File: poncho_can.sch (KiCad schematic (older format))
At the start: 15 parts

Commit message: Agrego la proteccion en el esquematico
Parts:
- removed J? (x4): GS2, Connectors:GS2, symbol GS2
- removed J? (x2): DB9_Female, symbol DB9_Female
- removed R? (x2): R, symbol R
- removed U? (x2): TJA1051T, Housings_SOIC:SOIC-8_3.9x4.9mm_Pitch1.27mm, symbol TJA1051T
- added C? (x2): 47n, symbol C
- added C?: 100n, symbol C
- added D?: A00094, symbol A00094
- added J? (x2): GS2, Connectors:GS2, symbol GS2
- added J?: DB9_Male_MountingHoles, symbol DB9_Male_MountingHoles
- added R? (x4): 60, symbol R
- added U?: TJA1051T, Housings_SOIC:SOIC-8_3.9x4.9mm_Pitch1.27mm, symbol TJA1051T
- gave numbers to parts that had none: 4
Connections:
- wire segments 88 -> 89
- no-connect marks 46 -> 45
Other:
- moved on the sheet: J10, J7, J8, J9, XA101B

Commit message: Improved PCB
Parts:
- added C103, C104: 47n, Capacitors_SMD:C_0805_HandSoldering, symbol C
- added C106: 100n, Capacitors_SMD:C_0805_HandSoldering, symbol C
- added D102: RSB27C2, TO_SOT_Packages_SMD:SOT-23W_Handsoldering, symbol A00094
- added J102: DB9_Male_MountingHoles, Connect:DB9MC, symbol DB9_Male_MountingHoles
- added J105, J106: GS2, Connect:GS2, symbol GS2
- added R103, R104, R107, R108: 60, Resistors_SMD:R_0805_HandSoldering, symbol R
- added U102: TJA1051T, Housings_SOIC:SOIC-8_3.9x4.9mm_Pitch1.27mm, symbol TJA1051T
- C101, C102, C105: renamed from C?; footprint (none) -> Capacitors_SMD:C_0805_HandSoldering
- D101: renamed from D?; value A00094 -> RSB27C2; footprint (none) -> TO_SOT_Packages_SMD:SOT-23; ManufacturerPN D5V0L2B3W-7 -> (none); Reverse Working Voltage 5V -> (none); eAPN A00094 -> (none)
- J10, J7, J8, J9: footprint Connectors:GS2 -> Connect:GS2
- J101: renamed from J?; footprint (none) -> Connect:DB9MC
- J103, J104: renamed from J?; footprint Connectors:GS2 -> Connect:GS2
- R101, R102, R105, R106: renamed from R?; footprint (none) -> Resistors_SMD:R_0805_HandSoldering
- gave numbers to parts that had none: 1
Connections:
- net +5V: now also C106.1, U102.3 (VCC)
- net GND: now also C103.1, C104.2, C106.2, D102.3 (common), J102.3, U102.2 (GND)
- net at J8.2 (G2): now also U102.4 (RXD)
- net at J7.2 (G2): now also U102.1 (TXD)
- new net: D102.2 (A2), J102.2, R103.2, R104.2, U102.6 (CANL)
- new net: D102.1 (A1), J102.7, J105.1 (G1), J106.1 (G1), U102.7 (CANH)
- new net: J106.2 (G2), R108.1
- new net: J105.2 (G2), R107.1
- new net: C103.2, R103.1, R107.2
- new net: C104.1, R104.1, R108.2
- no-connect marks 45 -> 46

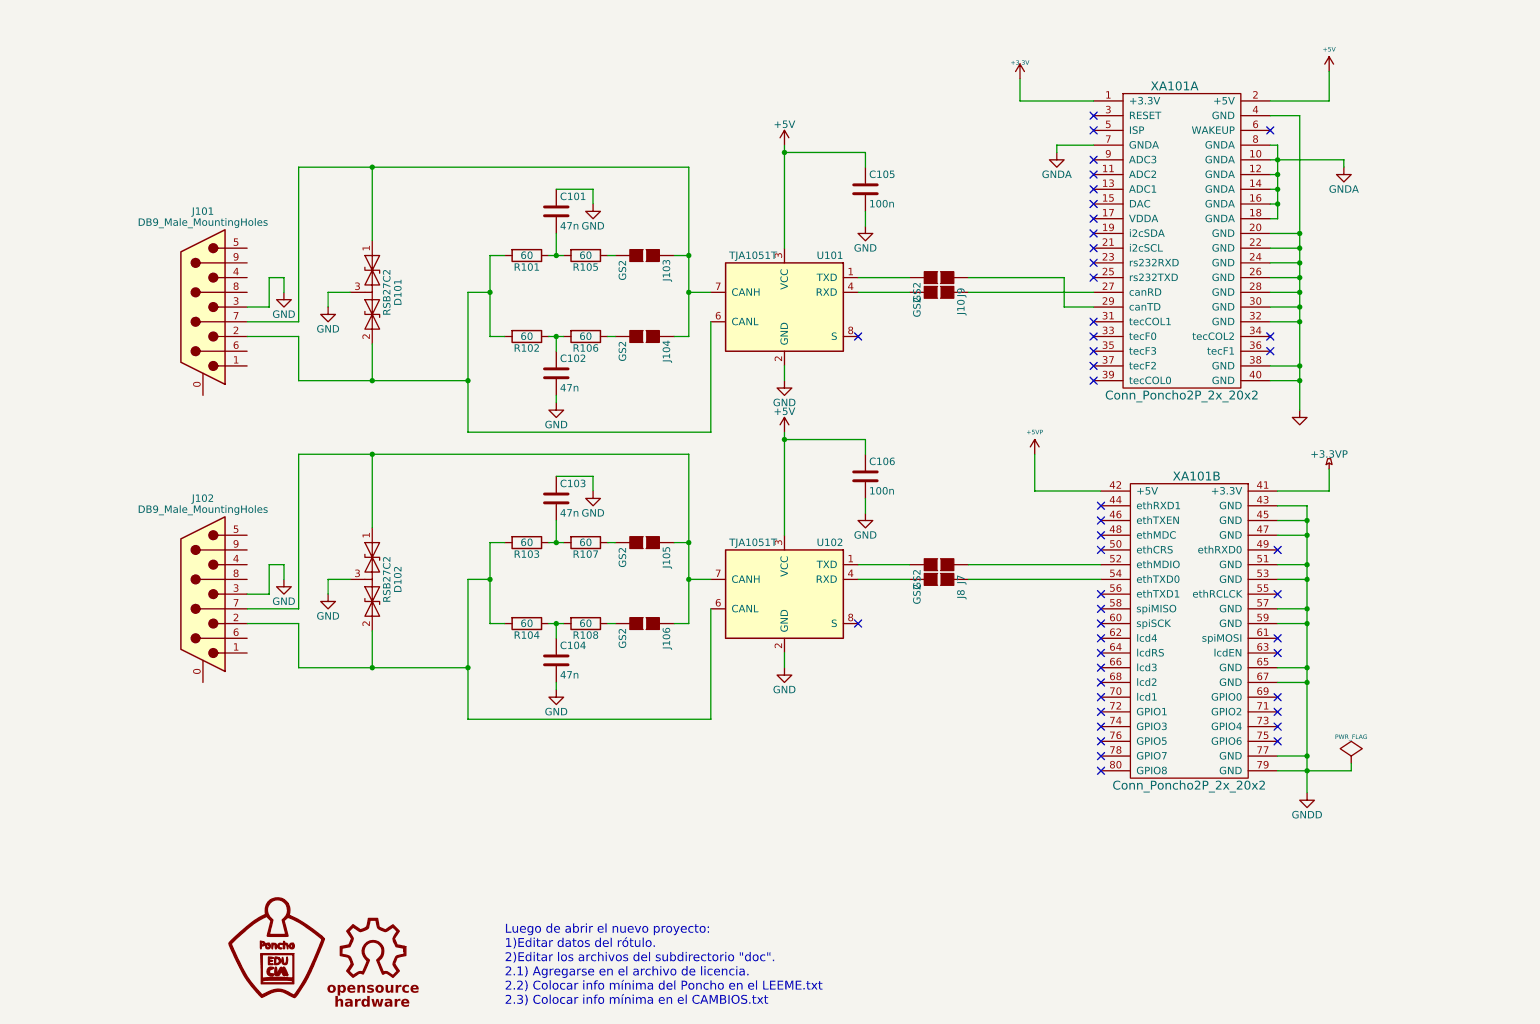
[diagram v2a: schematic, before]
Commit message: Cambio los jumpers de lugar en el esquematico y agrego leds en RX y TX
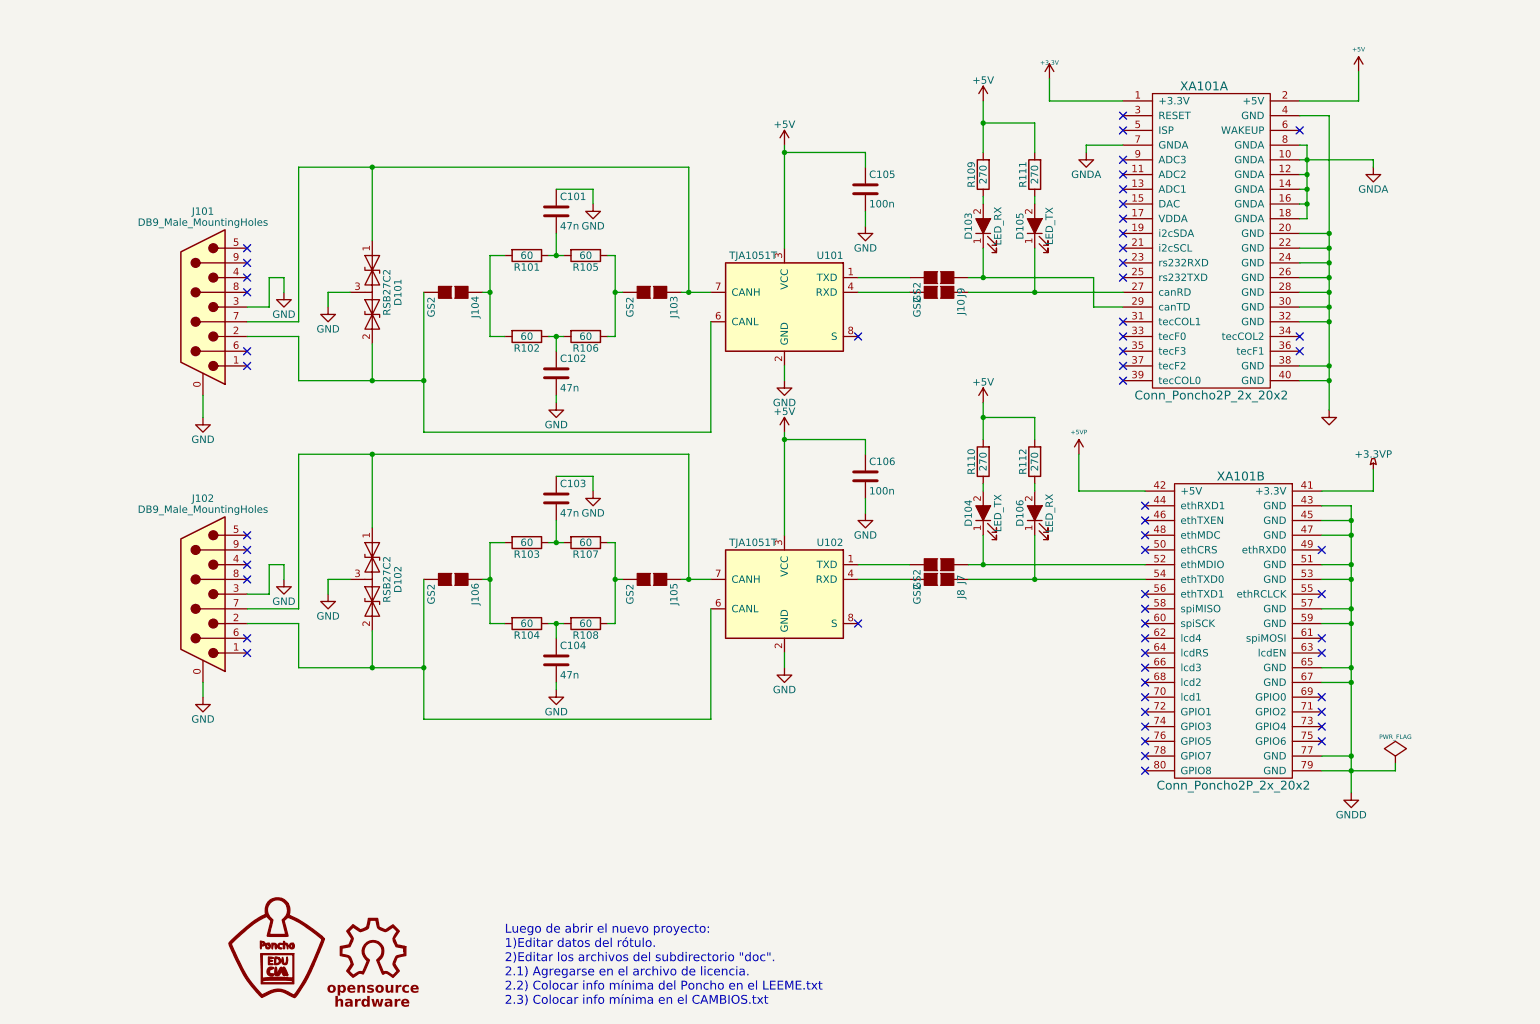
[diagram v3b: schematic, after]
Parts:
- added D103, D106: LED_RX, LEDs:LED_0805_HandSoldering, symbol LED_ALT
- added D104, D105: LED_TX, LEDs:LED_0805_HandSoldering, symbol LED_ALT
- added R109, R110, R111, R112: 270, Resistors_SMD:R_0805_HandSoldering, symbol R
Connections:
- net +5V: now also R109.2, R110.2, R111.2, R112.2
- net GND: now also J101.0 (PAD), J102.0 (PAD)
- net at J10.1 (G1), XA101.27 (canRD): now also D105.1 (K)
- net at J9.1 (G1), XA101.29 (canTD): now also D103.1 (K)
- net at J7.1 (G1), XA101.52 (ethMDIO): now also D104.1 (K)
- net at J8.1 (G1), XA101.54 (ethTXD0): now also D106.1 (K)
- net at D101.2 (A2), J101.2, U101.6 (CANL): now also J104.2 (G2); no longer R101.2, R102.2
- net at D101.1 (A1), J101.7, J103.1 (G1)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: no longer J104.1 (G1)
- net at R106.1: now also J103.2 (G2), R105.1; no longer J104.2 (G2)
- net at D102.2 (A2), J102.2, U102.6 (CANL): now also J106.2 (G2); no longer R103.2, R104.2
- net at D102.1 (A1), J102.7, J105.1 (G1)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: no longer J106.1 (G1)
- net at R108.1: now also J105.2 (G2), R107.1; no longer J106.2 (G2)
- new net: J104.1 (G1), R101.2, R102.2
- new net: J106.1 (G1), R103.2, R104.2
- new net: D103.2 (A), R109.1
- new net: D105.2 (A), R111.1
- new net: D104.2 (A), R110.1
- new net: D106.2 (A), R112.1
- no-connect marks 46 -> 58
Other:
- moved on the sheet: J103, J104, J105, J106, XA101A, XA101B

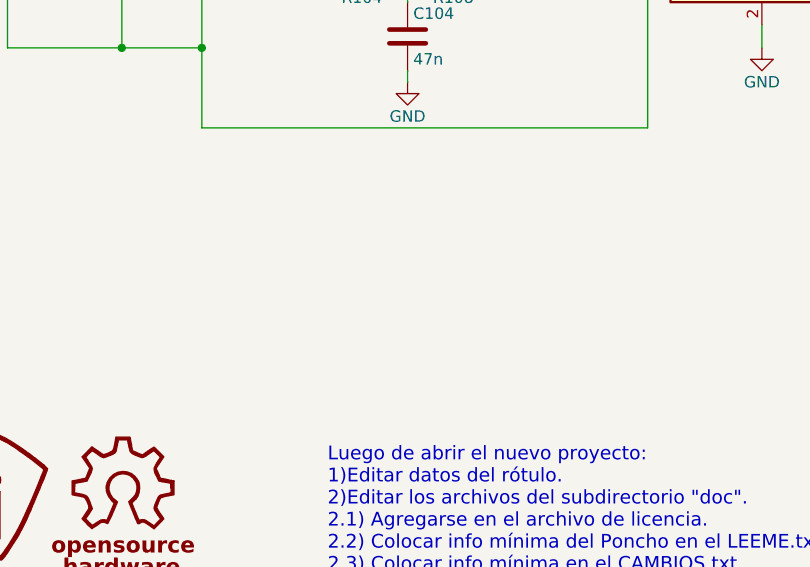
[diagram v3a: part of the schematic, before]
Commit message: Agreo la interconexion de las masas y las alimentaciones que habia borrado
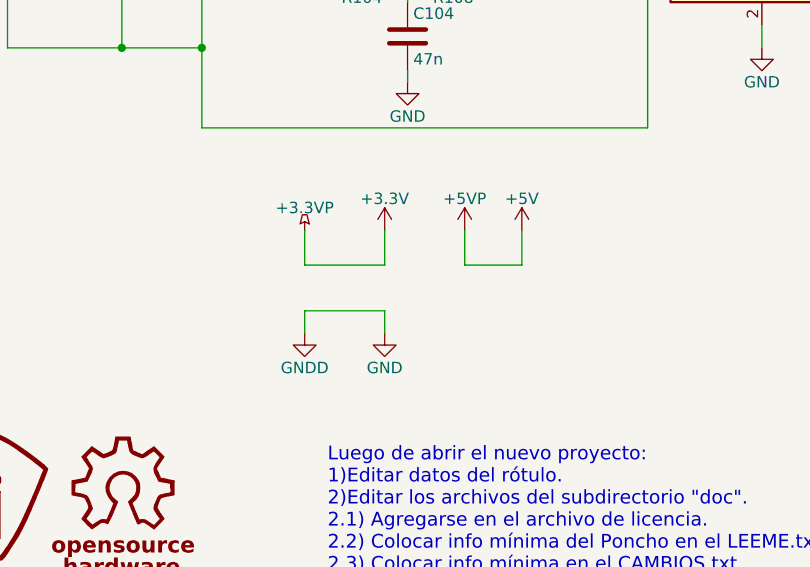
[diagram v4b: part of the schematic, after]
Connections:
- net +3V3 is gone; now on net +3.3VP: XA101.1 (+3.3V)
- net +5VP is gone; now on net +5V: XA101.42 (+5V)
- net GNDD is gone; now on net GND: XA101.43 (GND), XA101.45 (GND), XA101.47 (GND), XA101.51 (GND), XA101.53 (GND), XA101.57 (GND), XA101.59 (GND), XA101.65 (GND), XA101.67 (GND), XA101.77 (GND), XA101.79 (GND)
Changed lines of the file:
@@
 	5450 3700 5450 4550
 Connection ~ 5450 4550
+$Comp
+L +3.3VP #PWR028
+U 1 1 5BBC9D66
+P 4100 5950
+F 0 "#PWR028" H 4250 5900 50  0001 C CNN
+F 1 "+3.3VP" H 4100 6050 50  0000 C CNN
+F 2 "" H 4100 5950 50  0000 C CNN
+F 3 "" H 4100 5950 50  0000 C CNN
+	1    4100 5950
+	1    0    0    -1
+$EndComp
+$Comp
+L +3.3V #PWR029
+U 1 1 5BBC9DC6
+P 4450 5950
+F 0 "#PWR029" H 4450 5800 50  0001 C CNN
+F 1 "+3.3V" H 4450 6090 50  0000 C CNN
+F 2 "" H 4450 5950 50  0000 C CNN
+F 3 "" H 4450 5950 50  0000 C CNN
+	1    4450 5950
+	1    0    0    -1
+$EndComp
+$Comp
+L +5VP #PWR030
+U 1 1 5BBC9E26
+P 4800 5950
+F 0 "#PWR030" H 4800 5800 50  0001 C CNN
+F 1 "+5VP" H 4800 6090 50  0000 C CNN
+F 2 "" H 4800 5950 50  0000 C CNN
+F 3 "" H 4800 5950 50  0000 C CNN
+	1    4800 5950
+	1    0    0    -1
+$EndComp
+$Comp
+L +5V #PWR031
+U 1 1 5BBC9E86
+P 5050 5950
+F 0 "#PWR031" H 5050 5800 50  0001 C CNN
+F 1 "+5V" H 5050 6090 50  0000 C CNN
+F 2 "" H 5050 5950 50  0000 C CNN
+F 3 "" H 5050 5950 50  0000 C CNN
+	1    5050 5950
+	1    0    0    -1
+$EndComp
+$Comp
+L GNDD #PWR032
+U 1 1 5BBC9EE6
+P 4100 6400
+F 0 "#PWR032" H 4100 6150 50  0001 C CNN
+F 1 "GNDD" H 4100 6250 50  0000 C CNN
+F 2 "" H 4100 6400 50  0000 C CNN
+F 3 "" H 4100 6400 50  0000 C CNN
+	1    4100 6400
+	1    0    0    -1
+$EndComp
+$Comp
+L GND #PWR033
+U 1 1 5BBC9F46
+P 4450 6400
+F 0 "#PWR033" H 4450 6150 50  0001 C CNN
+F 1 "GND" H 4450 6250 50  0000 C CNN
+F 2 "" H 4450 6400 50  0000 C CNN
+F 3 "" H 4450 6400 50  0000 C CNN
+	1    4450 6400
+	1    0    0    -1
+$EndComp
+Wire Wire Line
+	4100 6400 4100 6300
+Wire Wire Line
+	4100 6300 4450 6300
+Wire Wire Line
+	4450 6300 4450 6400
+Wire Wire Line
+	4100 5950 4100 6100
+Wire Wire Line
+	4100 6100 4450 6100
+Wire Wire Line
+	4450 6100 4450 5950
+Wire Wire Line
+	4800 5950 4800 6100
+Wire Wire Line
+	4800 6100 5050 6100
+Wire Wire Line
+	5050 6100 5050 5950
 $EndSCHEMATC

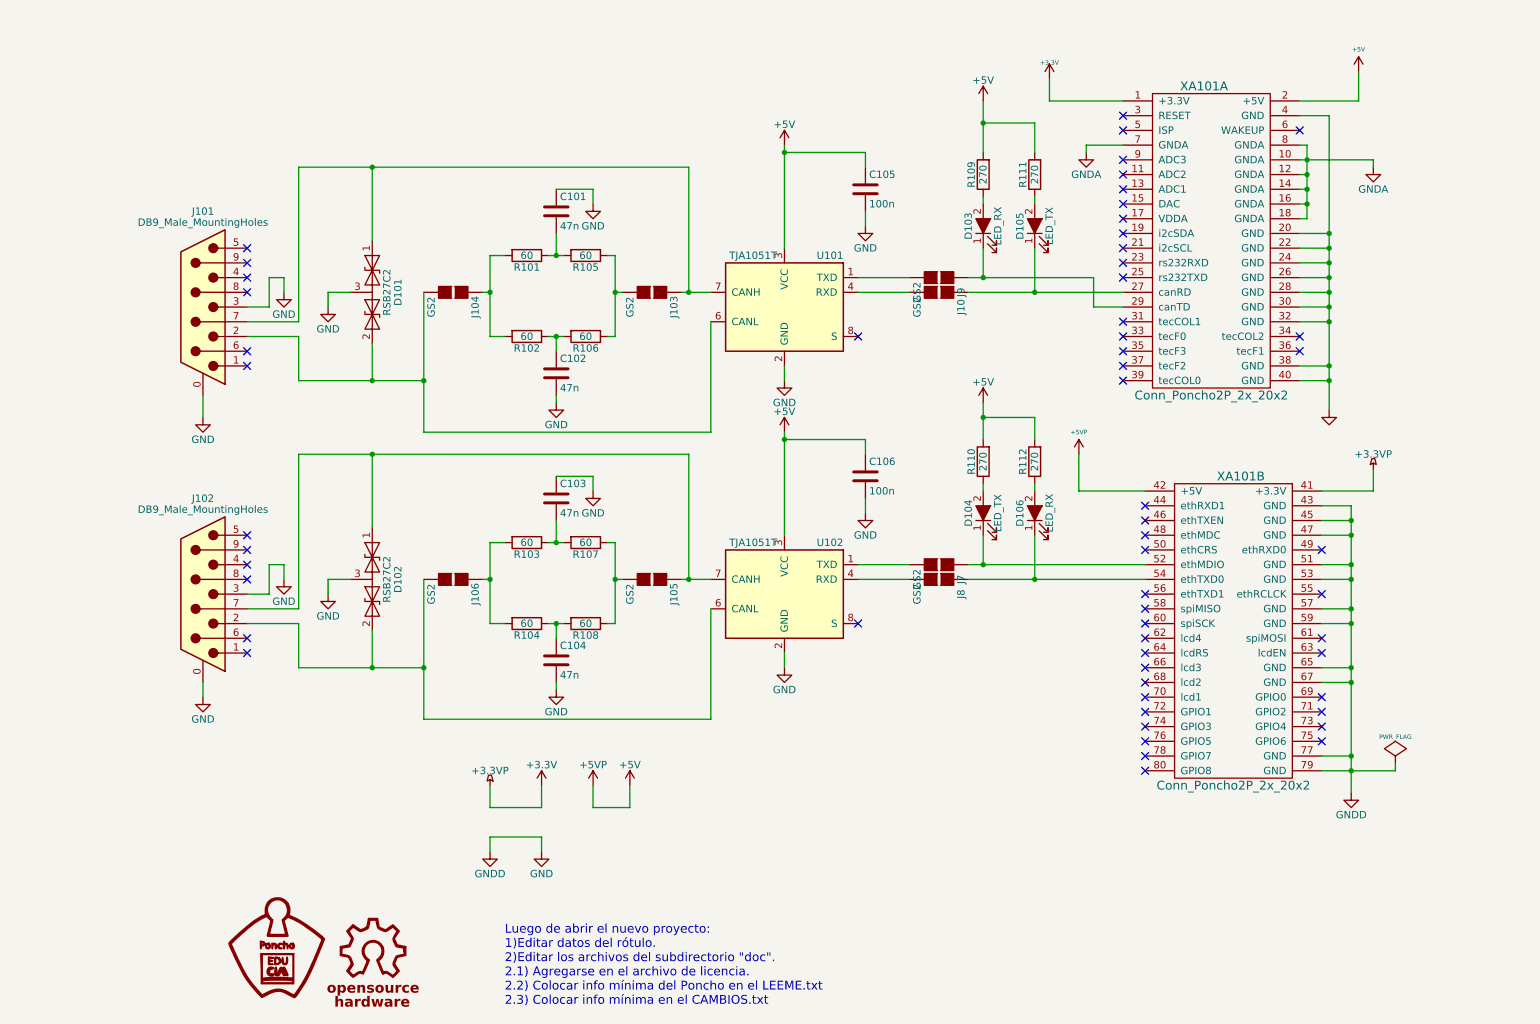
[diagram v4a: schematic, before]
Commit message: Agrego en el esquematico las señales de CAN como par diferencial
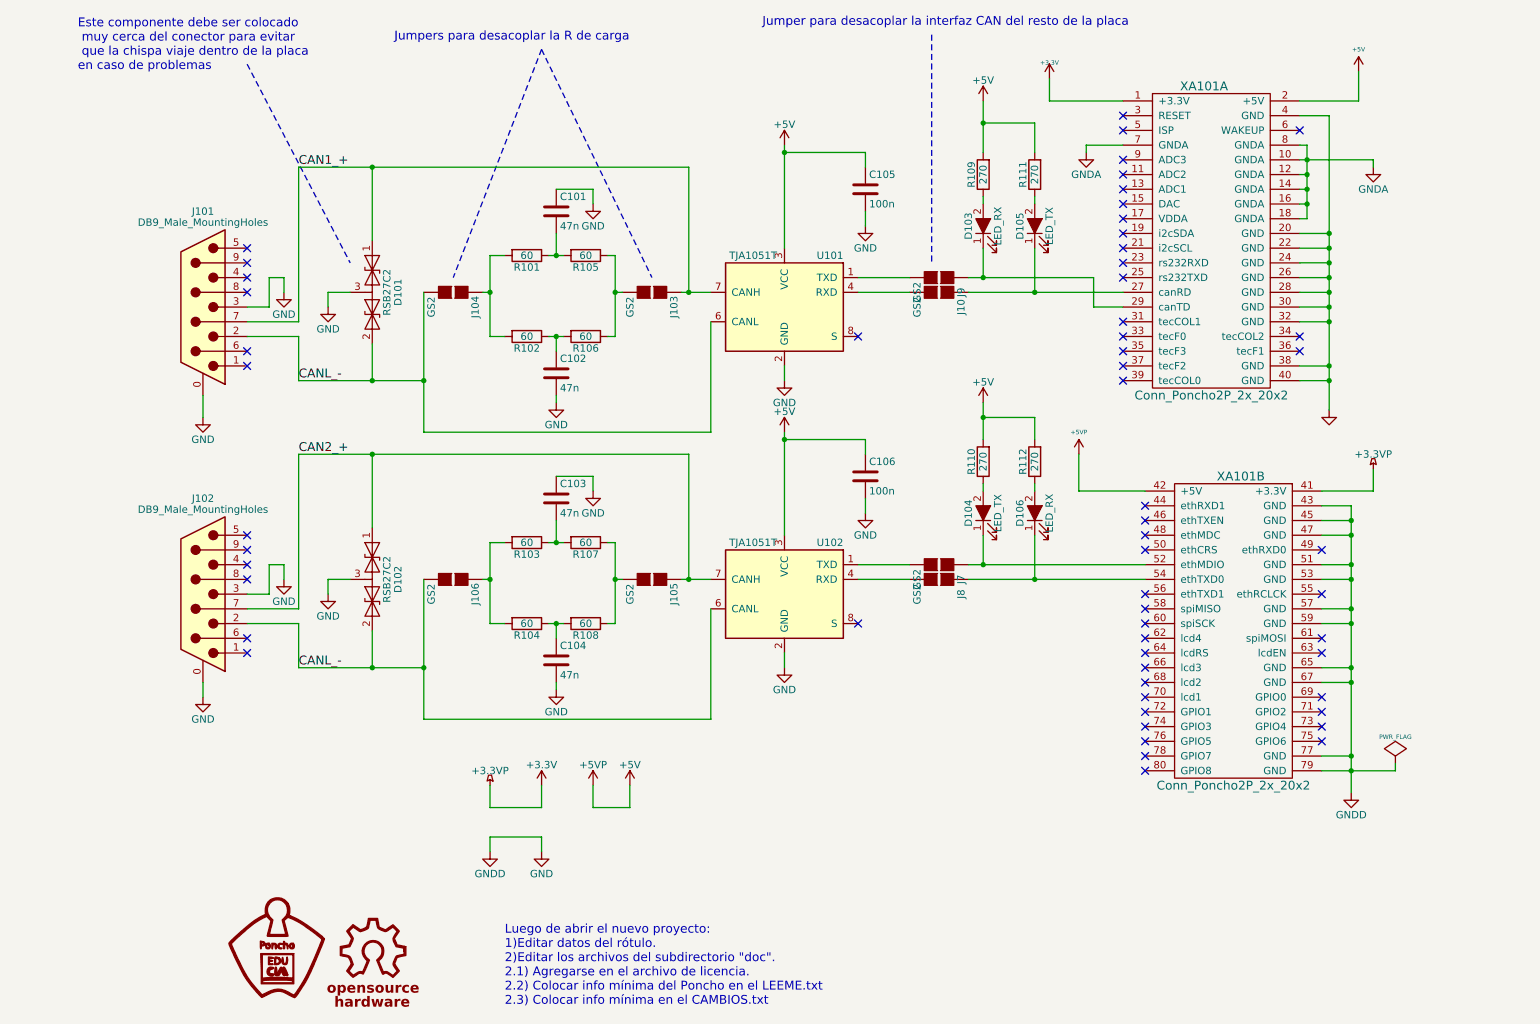
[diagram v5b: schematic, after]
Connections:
- net CANL_-: now reaches D101.2 (A2), J101.2, J104.2 (G2), U101.6 (CANL)
- net CANL_-: now also D102.2 (A2), J102.2, J106.2 (G2), U102.6 (CANL)
- net CAN1_+: now reaches D101.1 (A1), J101.7, J103.1 (G1), U101.7 (CANH)
- net CAN2_+: now reaches D102.1 (A1), J102.7, J105.1 (G1), U102.7 (CANH)
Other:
- note added: "Este componente debe ser colocado\n muy cerca del conector para evitar\n que la chispa viaje dentro de la placa \nen caso de problemas"
- note added: "Jumper para desacoplar la interfaz CAN del resto de la placa"
- note added: "Jumpers para desacoplar la R de carga"
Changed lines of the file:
@@
 Wire Wire Line
 	5050 6100 5050 5950
+Text Notes 1300 1100 0    60   ~ 0
+Este componente debe ser colocado\n muy cerca del conector para evitar\n que la chispa viaje dentro de la placa \nen caso de problemas
+Wire Notes Line
+	2450 1050 3150 2400
+Text Notes 3450 900  0    60   ~ 0
+Jumpers para desacoplar la R de carga
+Wire Notes Line
+	4450 950  3850 2500
+Wire Notes Line
+	4450 950  5200 2500
+Text Notes 5950 800  0    60   ~ 0
+Jumper para desacoplar la interfaz CAN del resto de la placa
+Wire Notes Line
+	7100 850  7100 2400
+Text Label 2800 3700 0    60   ~ 0
+CAN2_+
+Text Label 2800 5150 0    60   ~ 0
+CANL_-
+Text Label 2800 1750 0    60   ~ 0
+CAN1_+
+Text Label 2800 3200 0    60   ~ 0
+CANL_-
 $EndSCHEMATC
